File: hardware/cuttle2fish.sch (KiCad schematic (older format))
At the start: 25 parts, among them J1 USB_A, J2 CONN_01X05, J3 CONN_01x05, SW1 SW_SPST, U1 LP2985-3.3, U2 STM32F103R(8-B)Tx, U3 APA102-2020, U4 APA102-2020, Y1 10pF

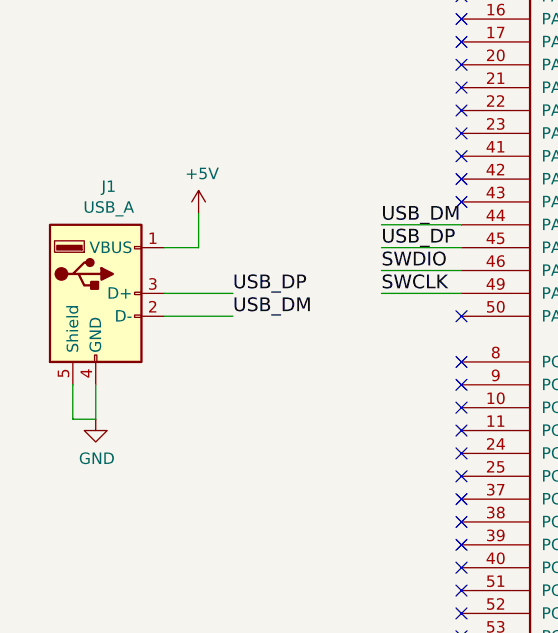
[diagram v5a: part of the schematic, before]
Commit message: Add PCB USB footprint and symbol from USBArmory
https://github.com/inversepath/usbarmory
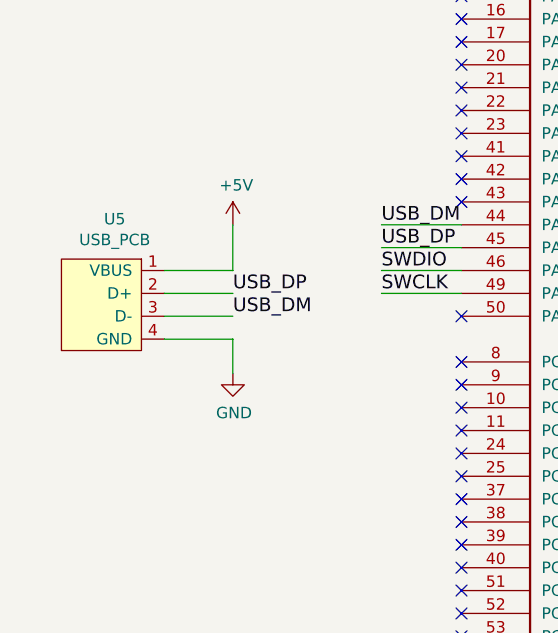
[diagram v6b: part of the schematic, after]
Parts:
- removed J1: USB_A, symbol Connector:USB_A
- added U5: USB_PCB, footprints:usb-PCB, symbol test:USB_PCB
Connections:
- net +5V: now also U5.1 (VBUS)
- net GND: now also U5.4 (GND)
- net USB_DM: now also U5.3 (D-)
- net USB_DP: now also U5.2 (D+)
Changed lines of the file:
@@
 L power:GND #PWR02
 U 1 1 5BF38602
-P 1000 2850
-F 0 "#PWR02" H 1000 2600 50  0001 C CNN
-F 1 "GND" H 1005 2677 50  0000 C CNN
-F 2 "" H 1000 2850 50  0001 C CNN
-F 3 "" H 1000 2850 50  0001 C CNN
-	1    1000 2850
+P 1600 2650
+F 0 "#PWR02" H 1600 2400 50  0001 C CNN
+F 1 "GND" H 1605 2477 50  0000 C CNN
+F 2 "" H 1600 2650 50  0001 C CNN
+F 3 "" H 1600 2650 50  0001 C CNN
+	1    1600 2650
 	1    0    0    -1
 $EndComp
@@
 L power:+5V #PWR06
 U 1 1 5BF386CE
-P 1450 1950
-F 0 "#PWR06" H 1450 1800 50  0001 C CNN
-F 1 "+5V" H 1465 2123 50  0000 C CNN
-F 2 "" H 1450 1950 50  0001 C CNN
-F 3 "" H 1450 1950 50  0001 C CNN
-	1    1450 1950
+P 1600 2000
+F 0 "#PWR06" H 1600 1850 50  0001 C CNN
+F 1 "+5V" H 1615 2173 50  0000 C CNN
+F 2 "" H 1600 2000 50  0001 C CNN
+F 3 "" H 1600 2000 50  0001 C CNN
+	1    1600 2000
 	1    0    0    -1
 $EndComp
@@
 	2600 4500 1550 4500
 Connection ~ 1550 4500
-Wire Wire Line
-	900  2700 900  2850
-Wire Wire Line
-	900  2850 1000 2850
-Wire Wire Line
-	1000 2850 1000 2700
-Wire Wire Line
-	1300 2100 1450 2100
-Wire Wire Line
-	1450 2100 1450 1950
 Wire Wire Line
 	1300 2400 1600 2400
@@
 Wire Wire Line
 	1000 4400 2600 4400
-$Comp
-L Connector:USB_A J1
-U 1 1 5BFA1B58
-P 1000 2300
-F 0 "J1" H 1057 2767 50  0000 C CNN
-F 1 "USB_A" H 1057 2676 50  0000 C CNN
-F 2 "" H 1150 2250 50  0001 C CNN
-F 3 " ~" H 1150 2250 50  0001 C CNN
-	1    1000 2300
-	1    0    0    -1
-$EndComp
 $Comp
 L Regulator_Linear:LP2985-3.3 U1
@@
 Wire Wire Line
 	10600 3650 10600 4000
+$Comp
+L test:USB_PCB U5
+U 1 1 5C104E8C
+P 1150 2050
+F 0 "U5" H 1083 2125 50  0000 C CNN
+F 1 "USB_PCB" H 1083 2034 50  0000 C CNN
+F 2 "footprints:usb-PCB" H 1150 2050 50  0001 C CNN
+F 3 "" H 1150 2050 50  0001 C CNN
+	1    1150 2050
+	1    0    0    -1
+$EndComp
+Wire Wire Line
+	1300 2500 1600 2500
+Wire Wire Line
+	1600 2500 1600 2650
+Wire Wire Line
+	1300 2200 1600 2200
+Wire Wire Line
+	1600 2200 1600 2000
 $EndSCHEMATC

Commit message: rename symbol file from test to symbols
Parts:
- U3, U4: symbol test:APA102_2020 -> symbols:APA102_2020
- U5: symbol test:USB_PCB -> symbols:USB_PCB
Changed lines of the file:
@@
 $EndComp
 $Comp
-L test:APA102_2020 U3
+L symbols:APA102_2020 U3
 U 1 1 5BFAAB90
 P 9000 5850
@@
 $EndComp
 $Comp
-L test:APA102_2020 U4
+L symbols:APA102_2020 U4
 U 1 1 5BFAB32A
 P 10000 5850
@@
 	10600 3650 10600 4000
 $Comp
-L test:USB_PCB U5
+L symbols:USB_PCB U5
 U 1 1 5C104E8C
 P 1150 2050

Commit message: add outline footprint and start routing!
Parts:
- J2, J3: footprint Socket_Strips:Socket_Strip_Straight_1x05_Pitch2.54mm -> footprints:Pin_Header_Straight_1x05_Pitch2.54mm
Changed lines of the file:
@@
 F 0 "J2" H 1878 6191 50  0000 L CNN
 F 1 "CONN_01X05" H 1878 6100 50  0000 L CNN
-F 2 "Socket_Strips:Socket_Strip_Straight_1x05_Pitch2.54mm" H 1800 6150 50  0001 C CNN
+F 2 "footprints:Pin_Header_Straight_1x05_Pitch2.54mm" H 1800 6150 50  0001 C CNN
 F 3 "" H 1800 6150 50  0001 C CNN
 	1    1800 6150
@@
 F 0 "J3" H 1878 7176 50  0000 L CNN
 F 1 "CONN_01x05" H 1878 7085 50  0000 L CNN
-F 2 "Socket_Strips:Socket_Strip_Straight_1x05_Pitch2.54mm" H 1850 7150 50  0001 C CNN
+F 2 "footprints:Pin_Header_Straight_1x05_Pitch2.54mm" H 1850 7150 50  0001 C CNN
 F 3 "~" H 1850 7150 50  0001 C CNN
 	1    1850 7150
